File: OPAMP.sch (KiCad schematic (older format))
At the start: 23 parts, among them P2 CONN_01X04, U6 TSV524A

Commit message: Complete... Still some things to check
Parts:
- C21, C22, C25, C26: value 18p -> 470p
- R29, R30, R31, R32: value ??? -> 5
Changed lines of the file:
@@
 EESchema Schematic File Version 2
+LIBS:Test_Board_MKE14F256-rescue
 LIBS:power
 LIBS:device
@@
 P 5885 2660
 F 0 "C21" H 5895 2730 50  0000 L CNN
-F 1 "18p" H 5895 2580 50  0000 L CNN
+F 1 "470p" H 5895 2580 50  0000 L CNN
 F 2 "Capacitors_SMD:C_0603" H 5885 2660 50  0001 C CNN
 F 3 "" H 5885 2660 50  0000 C CNN
@@
 P 13775 2660
 F 0 "C25" H 13785 2730 50  0000 L CNN
-F 1 "18p" H 13785 2580 50  0000 L CNN
+F 1 "470p" H 13785 2580 50  0000 L CNN
 F 2 "Capacitors_SMD:C_0603" H 13775 2660 50  0001 C CNN
 F 3 "" H 13775 2660 50  0000 C CNN
@@
 P 5930 6210
 F 0 "C22" H 5940 6280 50  0000 L CNN
-F 1 "18p" H 5940 6130 50  0000 L CNN
+F 1 "470p" H 5940 6130 50  0000 L CNN
 F 2 "Capacitors_SMD:C_0603" H 5930 6210 50  0001 C CNN
 F 3 "" H 5930 6210 50  0000 C CNN
@@
 P 13775 6160
 F 0 "C26" H 13785 6230 50  0000 L CNN
-F 1 "18p" H 13785 6080 50  0000 L CNN
+F 1 "470p" H 13785 6080 50  0000 L CNN
 F 2 "Capacitors_SMD:C_0603" H 13775 6160 50  0001 C CNN
 F 3 "" H 13775 6160 50  0000 C CNN
@@
 P 5670 2460
 F 0 "R29" V 5750 2460 50  0000 C CNN
-F 1 "???" V 5670 2460 50  0000 C CNN
+F 1 "5" V 5670 2460 50  0000 C CNN
 F 2 "Resistors_SMD:R_0603" V 5600 2460 50  0001 C CNN
 F 3 "" H 5670 2460 50  0000 C CNN
@@
 P 13580 2460
 F 0 "R31" V 13660 2460 50  0000 C CNN
-F 1 "???" V 13580 2460 50  0000 C CNN
+F 1 "5" V 13580 2460 50  0000 C CNN
 F 2 "Resistors_SMD:R_0603" V 13510 2460 50  0001 C CNN
 F 3 "" H 13580 2460 50  0000 C CNN
@@
 P 13580 5960
 F 0 "R32" V 13660 5960 50  0000 C CNN
-F 1 "???" V 13580 5960 50  0000 C CNN
+F 1 "5" V 13580 5960 50  0000 C CNN
 F 2 "Resistors_SMD:R_0603" V 13510 5960 50  0001 C CNN
 F 3 "" H 13580 5960 50  0000 C CNN
@@
 P 5735 6010
 F 0 "R30" V 5815 6010 50  0000 C CNN
-F 1 "???" V 5735 6010 50  0000 C CNN
+F 1 "5" V 5735 6010 50  0000 C CNN
 F 2 "Resistors_SMD:R_0603" V 5665 6010 50  0001 C CNN
 F 3 "" H 5735 6010 50  0000 C CNN

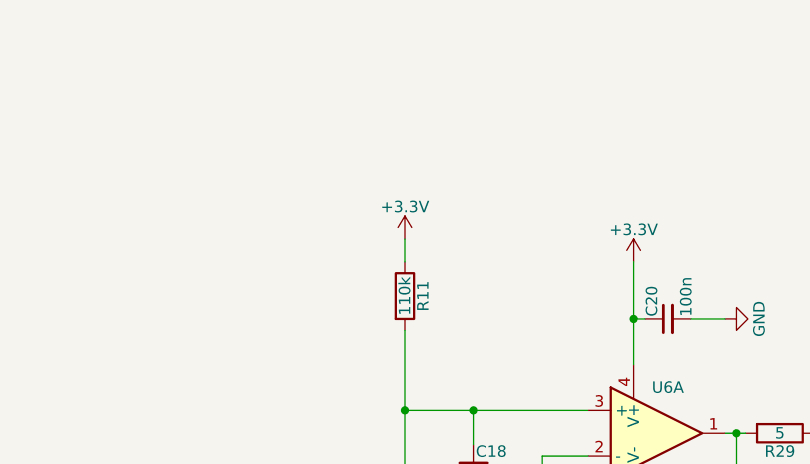
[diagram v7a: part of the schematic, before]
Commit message: corrected some mistakes listed in the email
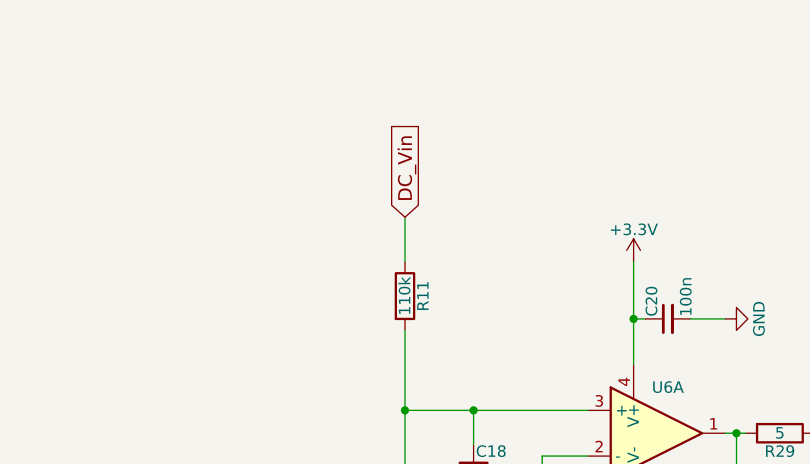
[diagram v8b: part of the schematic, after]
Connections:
- net +3V3: no longer R11.1
- new net DC_Vin: R11.1
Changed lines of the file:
@@
 $EndComp
 $Comp
-L +3.3V #PWR023
+L +3.3V #PWR28
 U 1 1 58BDE975
 P 5030 1710
-F 0 "#PWR023" H 5030 1560 50  0001 C CNN
+F 0 "#PWR28" H 5030 1560 50  0001 C CNN
 F 1 "+3.3V" H 5030 1850 50  0000 C CNN
 F 2 "" H 5030 1710 50  0000 C CNN
@@
 $EndComp
 $Comp
-L GND #PWR024
+L GND #PWR29
 U 1 1 58BDE976
 P 5030 3060
-F 0 "#PWR024" H 5030 2810 50  0001 C CNN
+F 0 "#PWR29" H 5030 2810 50  0001 C CNN
 F 1 "GND" H 5030 2910 50  0000 C CNN
 F 2 "" H 5030 3060 50  0000 C CNN
@@
 $EndComp
 $Comp
-L GND #PWR025
+L GND #PWR26
 U 1 1 58BDE977
 P 4330 3060
-F 0 "#PWR025" H 4330 2810 50  0001 C CNN
+F 0 "#PWR26" H 4330 2810 50  0001 C CNN
 F 1 "GND" H 4330 2910 50  0000 C CNN
 F 2 "" H 4330 3060 50  0000 C CNN
@@
 $EndComp
 $Comp
-L GND #PWR026
+L GND #PWR24
 U 1 1 58BDE978
 P 4030 3060
-F 0 "#PWR026" H 4030 2810 50  0001 C CNN
+F 0 "#PWR24" H 4030 2810 50  0001 C CNN
 F 1 "GND" H 4030 2910 50  0000 C CNN
 F 2 "" H 4030 3060 50  0000 C CNN
@@
 $EndComp
 $Comp
-L GND #PWR027
+L GND #PWR32
 U 1 1 58BDE979
 P 5430 1960
-F 0 "#PWR027" H 5430 1710 50  0001 C CNN
+F 0 "#PWR32" H 5430 1710 50  0001 C CNN
 F 1 "GND" H 5430 1810 50  0000 C CNN
 F 2 "" H 5430 1960 50  0000 C CNN
@@
 $EndComp
 $Comp
-L GND #PWR028
+L GND #PWR33
 U 1 1 58BDE97B
 P 5885 2810
-F 0 "#PWR028" H 5885 2560 50  0001 C CNN
+F 0 "#PWR33" H 5885 2560 50  0001 C CNN
 F 1 "GND" H 5885 2660 50  0000 C CNN
 F 2 "" H 5885 2810 50  0000 C CNN
@@
 $EndComp
 $Comp
-L +3.3V #PWR029
+L +3.3V #PWR39
 U 1 1 58BDE980
 P 12930 1710
-F 0 "#PWR029" H 12930 1560 50  0001 C CNN
+F 0 "#PWR39" H 12930 1560 50  0001 C CNN
 F 1 "+3.3V" H 12930 1850 50  0000 C CNN
 F 2 "" H 12930 1710 50  0000 C CNN
@@
 $EndComp
 $Comp
-L GND #PWR030
+L GND #PWR40
 U 1 1 58BDE981
 P 12930 3060
-F 0 "#PWR030" H 12930 2810 50  0001 C CNN
+F 0 "#PWR40" H 12930 2810 50  0001 C CNN
 F 1 "GND" H 12930 2910 50  0000 C CNN
 F 2 "" H 12930 3060 50  0000 C CNN
@@
 $EndComp
 $Comp
-L GND #PWR031
+L GND #PWR37
 U 1 1 58BDE982
 P 12230 3060
-F 0 "#PWR031" H 12230 2810 50  0001 C CNN
+F 0 "#PWR37" H 12230 2810 50  0001 C CNN
 F 1 "GND" H 12230 2910 50  0000 C CNN
 F 2 "" H 12230 3060 50  0000 C CNN
@@
 $EndComp
 $Comp
-L GND #PWR032
+L GND #PWR35
 U 1 1 58BDE983
 P 11930 3060
-F 0 "#PWR032" H 11930 2810 50  0001 C CNN
+F 0 "#PWR35" H 11930 2810 50  0001 C CNN
 F 1 "GND" H 11930 2910 50  0000 C CNN
 F 2 "" H 11930 3060 50  0000 C CNN
@@
 $EndComp
 $Comp
-L GND #PWR033
+L GND #PWR43
 U 1 1 58BDE985
 P 13775 2810
-F 0 "#PWR033" H 13775 2560 50  0001 C CNN
+F 0 "#PWR43" H 13775 2560 50  0001 C CNN
 F 1 "GND" H 13775 2660 50  0000 C CNN
 F 2 "" H 13775 2810 50  0000 C CNN
@@
 $EndComp
 $Comp
-L +3.3V #PWR034
+L +3.3V #PWR30
 U 1 1 58BDE98A
 P 5080 5260
-F 0 "#PWR034" H 5080 5110 50  0001 C CNN
+F 0 "#PWR30" H 5080 5110 50  0001 C CNN
 F 1 "+3.3V" H 5080 5400 50  0000 C CNN
 F 2 "" H 5080 5260 50  0000 C CNN
@@
 $EndComp
 $Comp
-L GND #PWR035
+L GND #PWR31
 U 1 1 58BDE98B
 P 5080 6610
-F 0 "#PWR035" H 5080 6360 50  0001 C CNN
+F 0 "#PWR31" H 5080 6360 50  0001 C CNN
 F 1 "GND" H 5080 6460 50  0000 C CNN
 F 2 "" H 5080 6610 50  0000 C CNN
@@
 $EndComp
 $Comp
-L GND #PWR036
+L GND #PWR27
 U 1 1 58BDE98C
 P 4380 6610
-F 0 "#PWR036" H 4380 6360 50  0001 C CNN
+F 0 "#PWR27" H 4380 6360 50  0001 C CNN
 F 1 "GND" H 4380 6460 50  0000 C CNN
 F 2 "" H 4380 6610 50  0000 C CNN
@@
 $EndComp
 $Comp
-L GND #PWR037
+L GND #PWR25
 U 1 1 58BDE98D
 P 4080 6610
-F 0 "#PWR037" H 4080 6360 50  0001 C CNN
+F 0 "#PWR25" H 4080 6360 50  0001 C CNN
 F 1 "GND" H 4080 6460 50  0000 C CNN
 F 2 "" H 4080 6610 50  0000 C CNN
@@
 $EndComp
 $Comp
-L GND #PWR038
+L GND #PWR34
 U 1 1 58BDE98F
 P 5930 6360
-F 0 "#PWR038" H 5930 6110 50  0001 C CNN
+F 0 "#PWR34" H 5930 6110 50  0001 C CNN
 F 1 "GND" H 5930 6210 50  0000 C CNN
 F 2 "" H 5930 6360 50  0000 C CNN
@@
 $EndComp
 $Comp
-L +3.3V #PWR039
+L +3.3V #PWR41
 U 1 1 58BDE994
 P 12930 5210
-F 0 "#PWR039" H 12930 5060 50  0001 C CNN
+F 0 "#PWR41" H 12930 5060 50  0001 C CNN
 F 1 "+3.3V" H 12930 5350 50  0000 C CNN
 F 2 "" H 12930 5210 50  0000 C CNN
@@
 $EndComp
 $Comp
-L GND #PWR040
+L GND #PWR42
 U 1 1 58BDE995
 P 12930 6560
-F 0 "#PWR040" H 12930 6310 50  0001 C CNN
+F 0 "#PWR42" H 12930 6310 50  0001 C CNN
 F 1 "GND" H 12930 6410 50  0000 C CNN
 F 2 "" H 12930 6560 50  0000 C CNN
@@
 $EndComp
 $Comp
-L GND #PWR041
+L GND #PWR38
 U 1 1 58BDE996
 P 12230 6560
-F 0 "#PWR041" H 12230 6310 50  0001 C CNN
+F 0 "#PWR38" H 12230 6310 50  0001 C CNN
 F 1 "GND" H 12230 6410 50  0000 C CNN
 F 2 "" H 12230 6560 50  0000 C CNN
@@
 $EndComp
 $Comp
-L GND #PWR042
+L GND #PWR36
 U 1 1 58BDE997
 P 11930 6560
-F 0 "#PWR042" H 11930 6310 50  0001 C CNN
+F 0 "#PWR36" H 11930 6310 50  0001 C CNN
 F 1 "GND" H 11930 6410 50  0000 C CNN
 F 2 "" H 11930 6560 50  0000 C CNN
@@
 $EndComp
 $Comp
-L GND #PWR043
+L GND #PWR44
 U 1 1 58BDE999
 P 13775 6310
-F 0 "#PWR043" H 13775 6060 50  0001 C CNN
+F 0 "#PWR44" H 13775 6060 50  0001 C CNN
 F 1 "GND" H 13775 6160 50  0000 C CNN
 F 2 "" H 13775 6310 50  0000 C CNN
@@
 V_in_3
 $Comp
-L +3.3V #PWR044
-U 1 1 58C3E0DE
-P 4030 1610
-F 0 "#PWR044" H 4030 1460 50  0001 C CNN
-F 1 "+3.3V" H 4030 1750 50  0000 C CNN
-F 2 "" H 4030 1610 50  0000 C CNN
-F 3 "" H 4030 1610 50  0000 C CNN
-	1    4030 1610
-	1    0    0    -1
-$EndComp
-$Comp
 L CONN_01X05 P2
 U 1 1 58C7A965
@@
 $EndComp
 $Comp
-L GND #PWR045
+L GND #PWR23
 U 1 1 58C7F1E0
 P 1270 4940
-F 0 "#PWR045" H 1270 4690 50  0001 C CNN
+F 0 "#PWR23" H 1270 4690 50  0001 C CNN
 F 1 "GND" H 1270 4790 50  0000 C CNN
 F 2 "" H 1270 4940 50  0000 C CNN
@@
 	4330 2710 4330 3060
 Wire Wire Line
-	4030 1710 4030 1610
+	4030 1515 4030 1710
 Connection ~ 5030 1960
 Wire Wire Line
@@
 Text GLabel 13380 5825 1    60   Input ~ 0
 OpAmp_Out4
+Text GLabel 4030 1515 1    60   Input ~ 0
+DC_Vin
 $EndSCHEMATC
